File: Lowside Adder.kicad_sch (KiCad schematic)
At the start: 6 parts, among them U4 VNL5090, U5 VNL5090, U6 VNL5090, U7 VNL5090

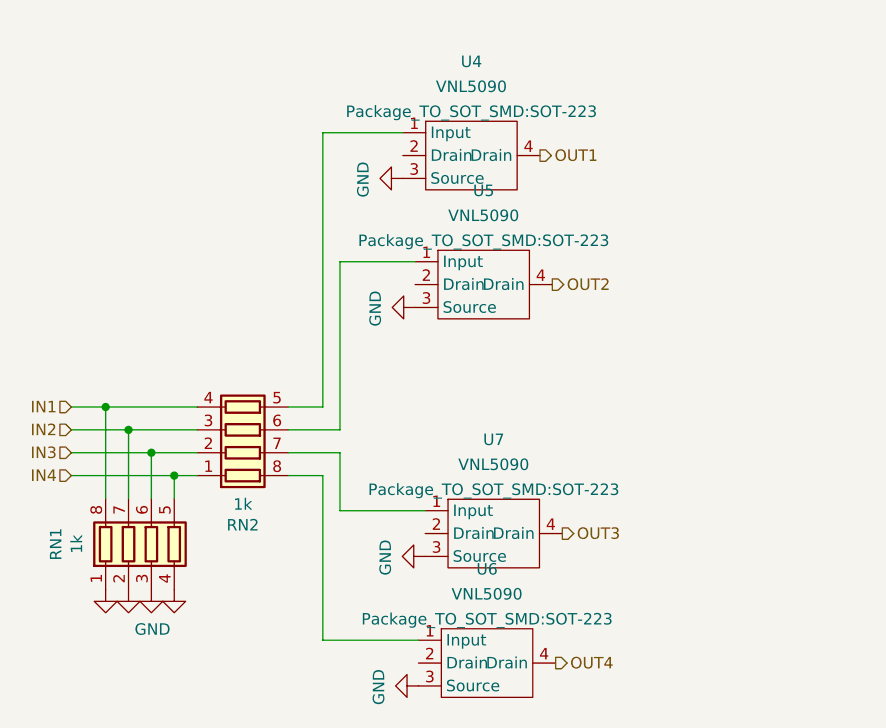
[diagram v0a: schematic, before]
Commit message: convert to kicad7, add jumpers for direct drive igbt output
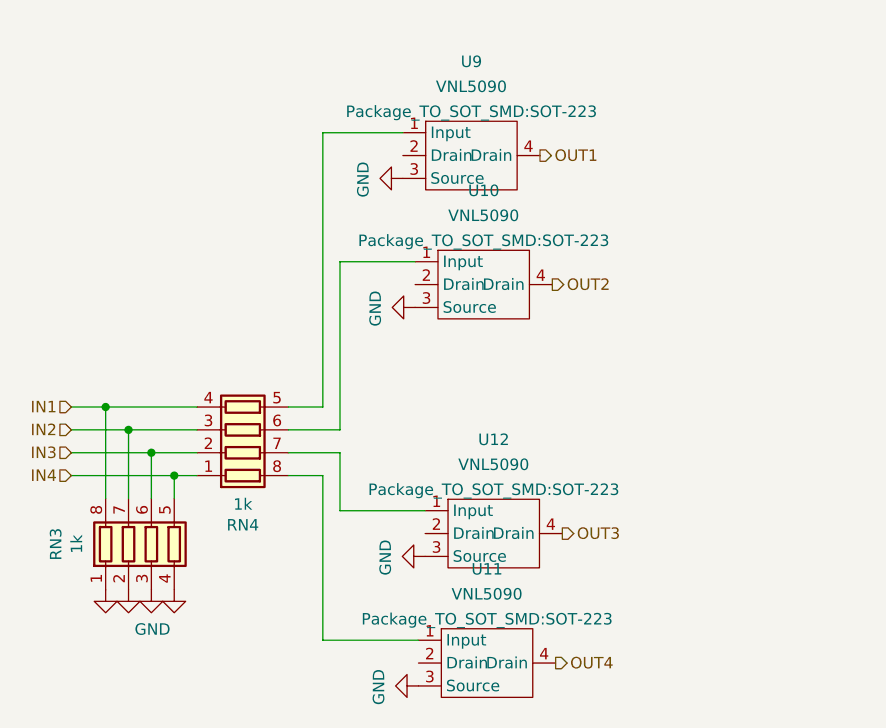
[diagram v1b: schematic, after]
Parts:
- renumbered RN1 to RN3, RN2 to RN4, U5 to U10, U6 to U11, U7 to U12, U4 to U9

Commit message: fix wideband library, ERC, DRC
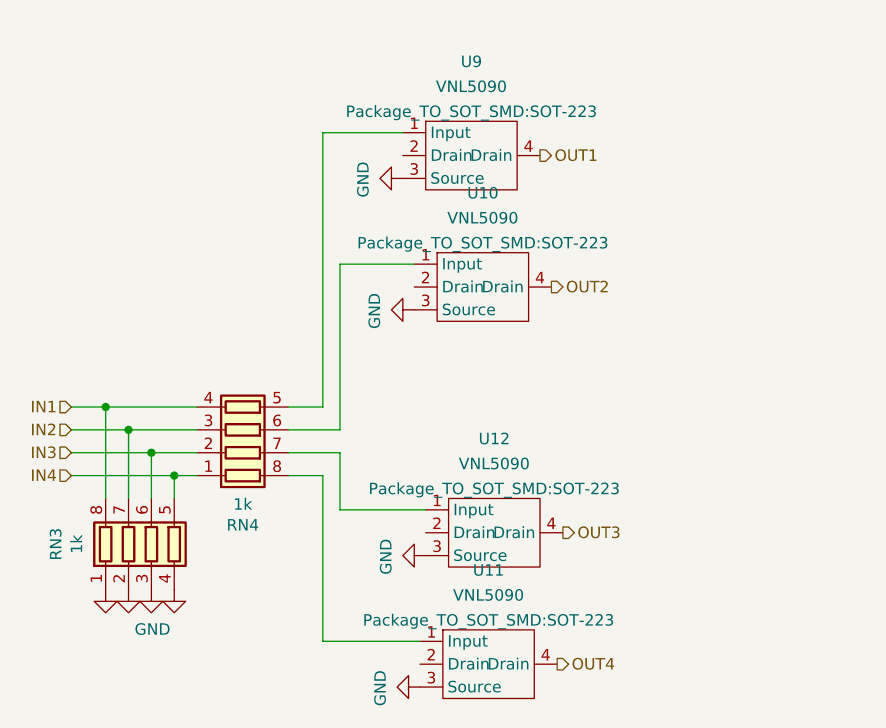
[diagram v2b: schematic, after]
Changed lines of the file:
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@@
     (stroke (width 0) (type default))
   )
-  (wire (pts (xy 129.481 92.7999) (xy 120.015 92.7999))
+  (wire (pts (xy 129.54 92.71) (xy 120.015 92.71))
     (stroke (width 0) (type default))
   )
@@
     (stroke (width 0) (type default))
   )
-  (wire (pts (xy 118.11 107.1901) (xy 128.7367 107.1901))
+  (wire (pts (xy 118.11 107.315) (xy 128.905 107.315))
     (stroke (width 0) (type default))
   )
@@
     (stroke (width 0) (type default))
   )
-  (wire (pts (xy 120.015 86.36) (xy 120.015 92.7999))
-    (stroke (width 0) (type default))
-  )
-  (wire (pts (xy 120.015 65.1359) (xy 128.3645 65.1359))
+  (wire (pts (xy 120.015 86.36) (xy 120.015 92.71))
+    (stroke (width 0) (type default))
+  )
+  (wire (pts (xy 120.015 65.405) (xy 128.27 65.405))
     (stroke (width 0) (type default))
   )
@@
     (stroke (width 0) (type default))
   )
-  (wire (pts (xy 118.11 88.9) (xy 118.11 107.1901))
-    (stroke (width 0) (type default))
-  )
-  (wire (pts (xy 120.015 65.1359) (xy 120.015 83.82))
-    (stroke (width 0) (type default))
-  )
-  (hierarchical_label "OUT4" (shape output) (at 143.9767 109.7301 0) (fields_autoplaced)
+  (wire (pts (xy 118.11 88.9) (xy 118.11 107.315))
+    (stroke (width 0) (type default))
+  )
+  (wire (pts (xy 120.015 65.405) (xy 120.015 83.82))
+    (stroke (width 0) (type default))
+  )
+  (hierarchical_label "OUT4" (shape output) (at 144.145 109.855 0) (fields_autoplaced)
     (effects (font (size 1.27 1.27)) (justify left))
   )
@@
     (effects (font (size 1.27 1.27)) (justify right))
   )
-  (hierarchical_label "OUT3" (shape output) (at 144.721 95.3399 0) (fields_autoplaced)
+  (hierarchical_label "OUT3" (shape output) (at 144.78 95.25 0) (fields_autoplaced)
     (effects (font (size 1.27 1.27)) (justify left))
   )
@@
     (effects (font (size 1.27 1.27)) (justify right))
   )
-  (hierarchical_label "OUT2" (shape output) (at 143.6045 67.6759 0) (fields_autoplaced)
+  (hierarchical_label "OUT2" (shape output) (at 143.51 67.945 0) (fields_autoplaced)
     (effects (font (size 1.27 1.27)) (justify left))
   )
@@
     (effects (font (size 1.27 1.27)) (justify left))
   )
-  (symbol (lib_id "Simon:VNL5090") (at 135.9845 65.1359 0) (unit 1)
+  (symbol (lib_id "Simon:VNL5090") (at 135.89 65.405 0) (unit 1)
     (in_bom yes) (on_board yes) (dnp no) (fields_autoplaced)
-    (property "Reference" "U10" (at 135.9845 57.2512 0)
-      (effects (font (size 1.27 1.27)))
-    )
-    (property "Value" "VNL5090" (at 135.9845 60.0263 0)
-      (effects (font (size 1.27 1.27)))
-    )
-    (property "Footprint" "Package_TO_SOT_SMD:SOT-223" (at 135.9845 62.8014 0)
-      (effects (font (size 1.27 1.27)))
-    )
-    (property "Datasheet" "" (at 135.9845 65.1359 0)
-      (effects (font (size 1.27 1.27)) hide)
-    )
-    (property "LCSC" "C2680415" (at 135.9845 65.1359 0)
+    (property "Reference" "U10" (at 135.89 57.5203 0)
+      (effects (font (size 1.27 1.27)))
+    )
+    (property "Value" "VNL5090" (at 135.89 60.2954 0)
+      (effects (font (size 1.27 1.27)))
+    )
+    (property "Footprint" "Package_TO_SOT_SMD:SOT-223" (at 135.89 63.0705 0)
+      (effects (font (size 1.27 1.27)))
+    )
+    (property "Datasheet" "" (at 135.89 65.405 0)
+      (effects (font (size 1.27 1.27)) hide)
+    )
+    (property "LCSC" "C2680415" (at 135.89 65.405 0)
       (effects (font (size 1.27 1.27)) hide)
     )
@@
     )
   )
-  (symbol (lib_id "Simon:VNL5090") (at 137.101 92.7999 0) (unit 1)
+  (symbol (lib_id "Simon:VNL5090") (at 137.16 92.71 0) (unit 1)
     (in_bom yes) (on_board yes) (dnp no) (fields_autoplaced)
-    (property "Reference" "U12" (at 137.101 84.9152 0)
-      (effects (font (size 1.27 1.27)))
-    )
-    (property "Value" "VNL5090" (at 137.101 87.6903 0)
-      (effects (font (size 1.27 1.27)))
-    )
-    (property "Footprint" "Package_TO_SOT_SMD:SOT-223" (at 137.101 90.4654 0)
-      (effects (font (size 1.27 1.27)))
-    )
-    (property "Datasheet" "" (at 137.101 92.7999 0)
-      (effects (font (size 1.27 1.27)) hide)
-    )
-    (property "LCSC" "C2680415" (at 137.101 92.7999 0)
+    (property "Reference" "U12" (at 137.16 84.8253 0)
+      (effects (font (size 1.27 1.27)))
+    )
+    (property "Value" "VNL5090" (at 137.16 87.6004 0)
+      (effects (font (size 1.27 1.27)))
+    )
+    (property "Footprint" "Package_TO_SOT_SMD:SOT-223" (at 137.16 90.3755 0)
+      (effects (font (size 1.27 1.27)))
+    )
+    (property "Datasheet" "" (at 137.16 92.71 0)
+      (effects (font (size 1.27 1.27)) hide)
+    )
+    (property "LCSC" "C2680415" (at 137.16 92.71 0)
       (effects (font (size 1.27 1.27)) hide)
     )
@@
     )
   )
-  (symbol (lib_id "power:GND") (at 129.481 97.8799 270) (unit 1)
-    (in_bom yes) (on_board yes) (dnp no)
-    (property "Reference" "#PWR061" (at 123.131 97.8799 0)
-      (effects (font (size 1.27 1.27)) hide)
-    )
-    (property "Value" "GND" (at 125.0868 98.0069 0)
-      (effects (font (size 1.27 1.27)))
-    )
-    (property "Footprint" "" (at 129.481 97.8799 0)
-      (effects (font (size 1.27 1.27)) hide)
-    )
-    (property "Datasheet" "" (at 129.481 97.8799 0)
+  (symbol (lib_id "power:GND") (at 129.54 97.79 270) (unit 1)
+    (in_bom yes) (on_board yes) (dnp no)
+    (property "Reference" "#PWR061" (at 123.19 97.79 0)
+      (effects (font (size 1.27 1.27)) hide)
+    )
+    (property "Value" "GND" (at 125.1458 97.917 0)
+      (effects (font (size 1.27 1.27)))
+    )
+    (property "Footprint" "" (at 129.54 97.79 0)
+      (effects (font (size 1.27 1.27)) hide)
+    )
+    (property "Datasheet" "" (at 129.54 97.79 0)
       (effects (font (size 1.27 1.27)) hide)
     )
@@
     )
   )
-  (symbol (lib_id "power:GND") (at 128.7367 112.2701 270) (unit 1)
-    (in_bom yes) (on_board yes) (dnp no)
-    (property "Reference" "#PWR060" (at 122.3867 112.2701 0)
-      (effects (font (size 1.27 1.27)) hide)
-    )
-    (property "Value" "GND" (at 124.3425 112.3971 0)
-      (effects (font (size 1.27 1.27)))
-    )
-    (property "Footprint" "" (at 128.7367 112.2701 0)
-      (effects (font (size 1.27 1.27)) hide)
-    )
-    (property "Datasheet" "" (at 128.7367 112.2701 0)
+  (symbol (lib_id "power:GND") (at 128.905 112.395 270) (unit 1)
+    (in_bom yes) (on_board yes) (dnp no)
+    (property "Reference" "#PWR060" (at 122.555 112.395 0)
+      (effects (font (size 1.27 1.27)) hide)
+    )
+    (property "Value" "GND" (at 124.5108 112.522 0)
+      (effects (font (size 1.27 1.27)))
+    )
+    (property "Footprint" "" (at 128.905 112.395 0)
+      (effects (font (size 1.27 1.27)) hide)
+    )
+    (property "Datasheet" "" (at 128.905 112.395 0)
       (effects (font (size 1.27 1.27)) hide)
     )
@@
     )
   )
-  (symbol (lib_id "power:GND") (at 128.3645 70.2159 270) (unit 1)
-    (in_bom yes) (on_board yes) (dnp no)
-    (property "Reference" "#PWR059" (at 122.0145 70.2159 0)
-      (effects (font (size 1.27 1.27)) hide)
-    )
-    (property "Value" "GND" (at 123.9703 70.3429 0)
-      (effects (font (size 1.27 1.27)))
-    )
-    (property "Footprint" "" (at 128.3645 70.2159 0)
-      (effects (font (size 1.27 1.27)) hide)
-    )
-    (property "Datasheet" "" (at 128.3645 70.2159 0)
+  (symbol (lib_id "power:GND") (at 128.27 70.485 270) (unit 1)
+    (in_bom yes) (on_board yes) (dnp no)
+    (property "Reference" "#PWR059" (at 121.92 70.485 0)
+      (effects (font (size 1.27 1.27)) hide)
+    )
+    (property "Value" "GND" (at 123.8758 70.612 0)
+      (effects (font (size 1.27 1.27)))
+    )
+    (property "Footprint" "" (at 128.27 70.485 0)
+      (effects (font (size 1.27 1.27)) hide)
+    )
+    (property "Datasheet" "" (at 128.27 70.485 0)
       (effects (font (size 1.27 1.27)) hide)
     )
@@
     )
   )
-  (symbol (lib_id "Simon:VNL5090") (at 136.3567 107.1901 0) (unit 1)
+  (symbol (lib_id "Simon:VNL5090") (at 136.525 107.315 0) (unit 1)
     (in_bom yes) (on_board yes) (dnp no) (fields_autoplaced)
-    (property "Reference" "U11" (at 136.3567 99.3054 0)
-      (effects (font (size 1.27 1.27)))
-    )
-    (property "Value" "VNL5090" (at 136.3567 102.0805 0)
-      (effects (font (size 1.27 1.27)))
-    )
-    (property "Footprint" "Package_TO_SOT_SMD:SOT-223" (at 136.3567 104.8556 0)
-      (effects (font (size 1.27 1.27)))
-    )
-    (property "Datasheet" "" (at 136.3567 107.1901 0)
-      (effects (font (size 1.27 1.27)) hide)
-    )
-    (property "LCSC" "C2680415" (at 136.3567 107.1901 0)
-      (effects (font (size 1.27 1.27)) hide)
-    )
+    (property "Reference" "U11" (at 136.525 99.4303 0)
+      (effects (font (size 1.27 1.27)))
+    )
+    (property "Value" "VNL5090" (at 136.525 102.2054 0)
+      (effects (font (size 1.27 1.27)))
+    )
+    (property "Footprint" "Package_TO_SOT_SMD:SOT-223" (at 136.525 104.9805 0)
+      (effects (font (size 1.27 1.27)))
+    )
+    (property "Datasheet" "" (at 136.525 107.315 0)
+      (effects (font (size 1.27 1.27)) hide)
+    )
+    (property "LCSC" "C2680415" (at 136.525 107.315 0)
+      (effects (font (size 1.27 1.27)) hide)
+    )

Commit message: Add freewheel diodes, power pins explanation comment
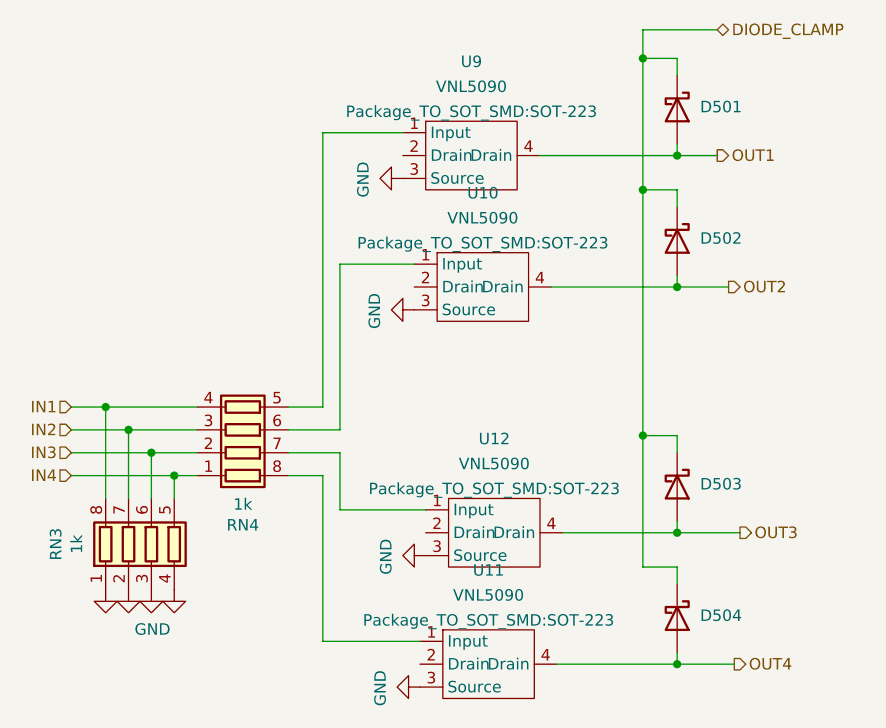
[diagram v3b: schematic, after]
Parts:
- added D501, D502, D503, D504: D_Schottky, Diode_SMD:D_SMA, symbol Device:D_Schottky
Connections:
- net OUT1: now also D501.2 (A)
- net OUT2: now also D502.2 (A)
- net OUT3: now also D503.2 (A)
- net OUT4: now also D504.2 (A)
- new net DIODE_CLAMP: D501.1 (K), D502.1 (K), D503.1 (K), D504.1 (K)

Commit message: schematic title blocks
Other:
- company: (none) -> FutureProofPerformance.com
- title: (none) -> Polygonus Universal 88p
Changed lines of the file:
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@@
 (kicad_sch (version 20230121) (generator eeschema)
   (paper "A4")
+  (title_block
+    (title "Polygonus Universal 88p")
+    (date "2023-11-12")
+    (rev "v1.0")
+    (company "FutureProofPerformance.com")
+  )
   (junction (at 99.06 86.36) (diameter 0) (color 0 0 0 0)
   )
